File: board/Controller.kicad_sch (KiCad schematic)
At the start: 25 parts, among them U2 MP8007, U3 POE30P-50L

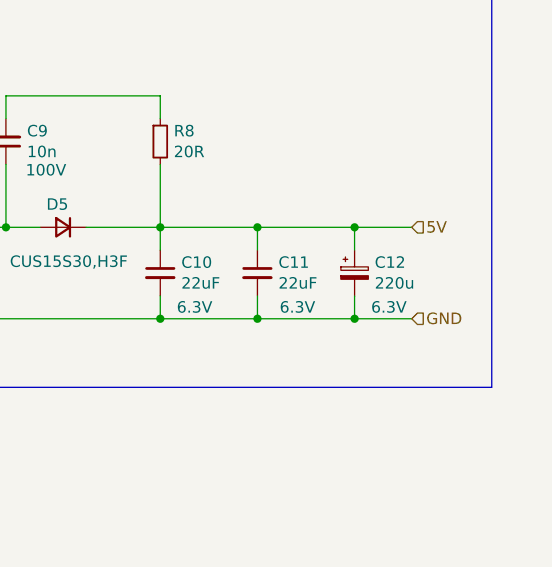
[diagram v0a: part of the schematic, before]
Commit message: added LDO
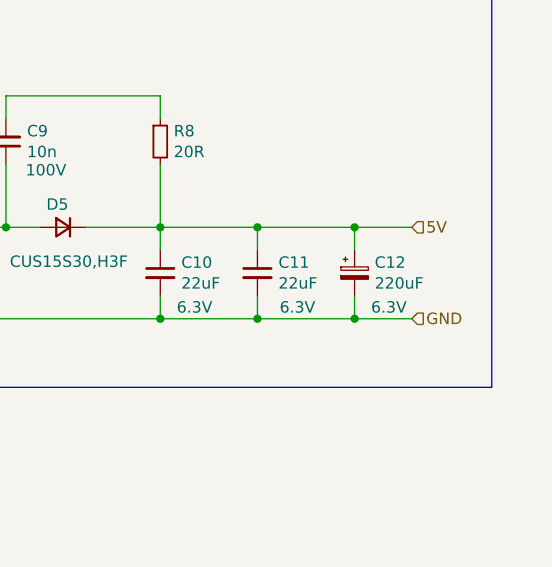
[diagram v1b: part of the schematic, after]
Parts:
- C12: value 220u -> 220uF; footprint Capacitor_Tantalum_SMD:CP_EIA-7343-31_Kemet-D -> Capacitor_SMD:CP_Elec_6.3x5.9; MPN (none) -> EEE-FK1C221XP

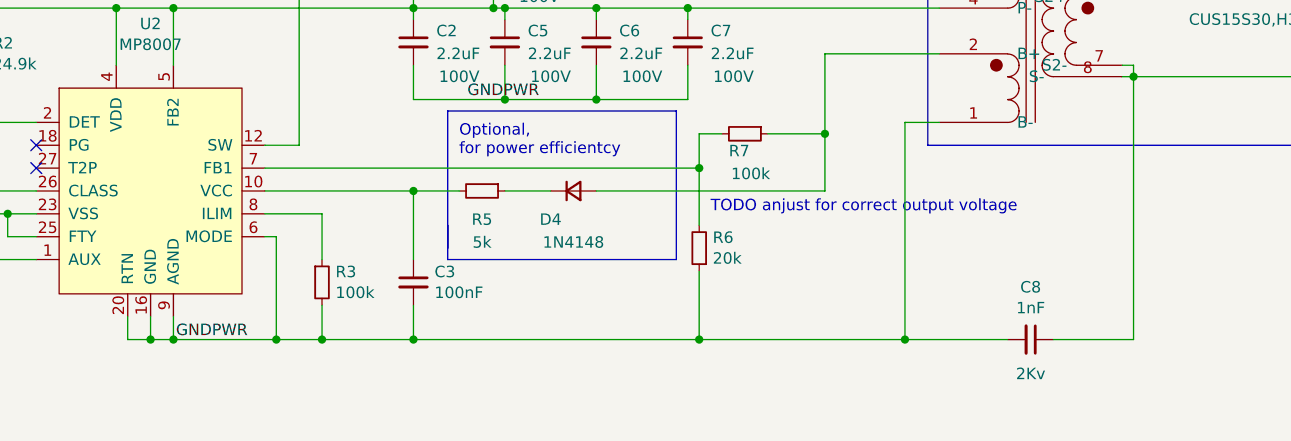
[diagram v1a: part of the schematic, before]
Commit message: tuned ILIM resistor and voltage divider of flyback
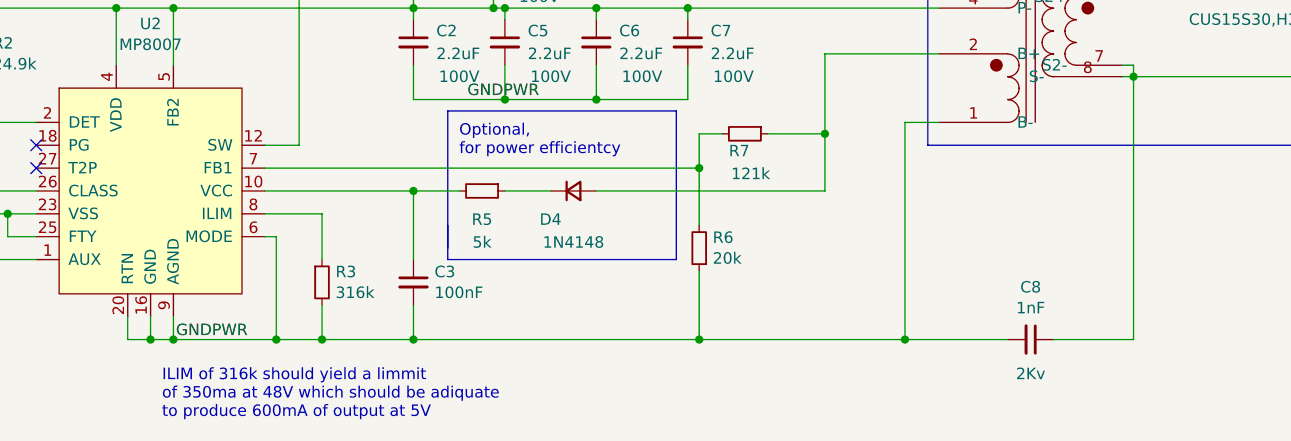
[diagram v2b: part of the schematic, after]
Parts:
- R3: value 100k -> 316k
- R7: value 100k -> 121k
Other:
- note added: "ILIM of 316k should yield a limmit of 350ma at 48V which should be adiquate to produce 600mA of output at 5V"
- note removed: "TODO anjust for correct output voltage"
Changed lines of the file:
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@@
     (effects (font (size 1.27 1.27)) (justify left bottom))
   )
-  (text "TODO anjust for correct output voltage" (at 165.1 92.71 0)
+  (text "ILIM of 316k should yield a limmit \nof 350ma at 48V which should be adiquate \nto produce 600mA of output at 5V"
+    (at 104.14 115.57 0)
     (effects (font (size 1.27 1.27)) (justify left bottom))
   )
@@
       (effects (font (size 1.27 1.27)) (justify left))
     )
-    (property "Value" "100k" (at 123.4186 101.473 0)
+    (property "Value" "316k" (at 123.4186 101.473 0)
       (effects (font (size 1.27 1.27)) (justify left))
     )
@@
       (effects (font (size 1.27 1.27)))
     )
-    (property "Value" "100k" (at 169.545 88.265 90)
-      (effects (font (size 1.27 1.27)))
-    )
+    (property "Value" "121k" (at 169.545 88.265 90)
+      (effects (font (size 1.27 1.27)))
+    )

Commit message: made bulk cap footprint larger
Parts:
- C12: footprint Capacitor_SMD:CP_Elec_6.3x5.9 -> Capacitor_SMD:CP_Elec_8x6.9
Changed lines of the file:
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@@
       (effects (font (size 1.27 1.27)) (justify left))
     )
-    (property "Footprint" "Capacitor_SMD:CP_Elec_6.3x5.9" (at 256.54 72.39 0)
+    (property "Footprint" "Capacitor_SMD:CP_Elec_8x6.9" (at 256.54 72.39 0)
       (effects (font (size 1.27 1.27)) hide)
     )

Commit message: improved docs for D4
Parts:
- D4: LCSC (none) -> C2128; MPN (none) -> 1N4148WS
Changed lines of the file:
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@@
+      (effects (font (size 1.27 1.27)) hide)
+    )
+    (property "MPN" "1N4148WS" (at 149.86 90.17 0)
+      (effects (font (size 1.27 1.27)) hide)
+    )
+    (property "LCSC" "C2128" (at 149.86 90.17 0)
       (effects (font (size 1.27 1.27)) hide)
     )

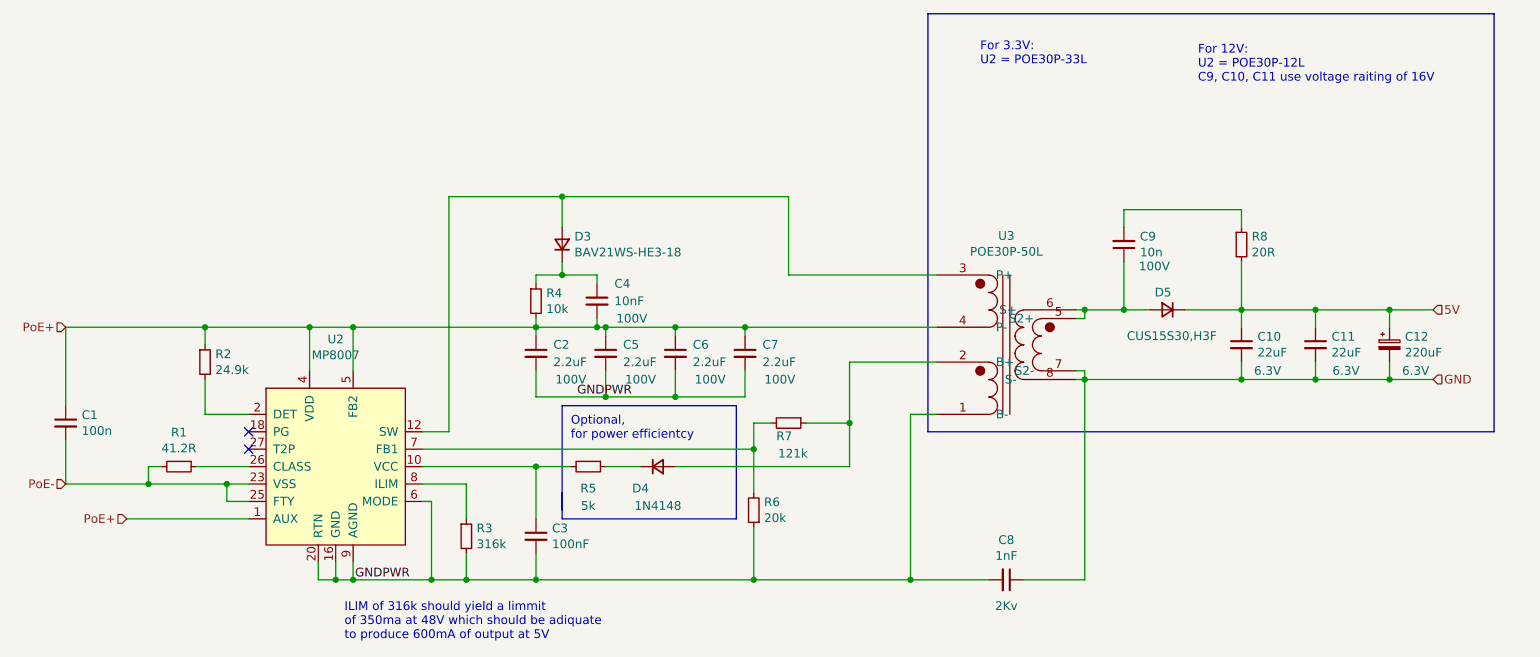
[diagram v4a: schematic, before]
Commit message: added pours for LDO and LCSC parts
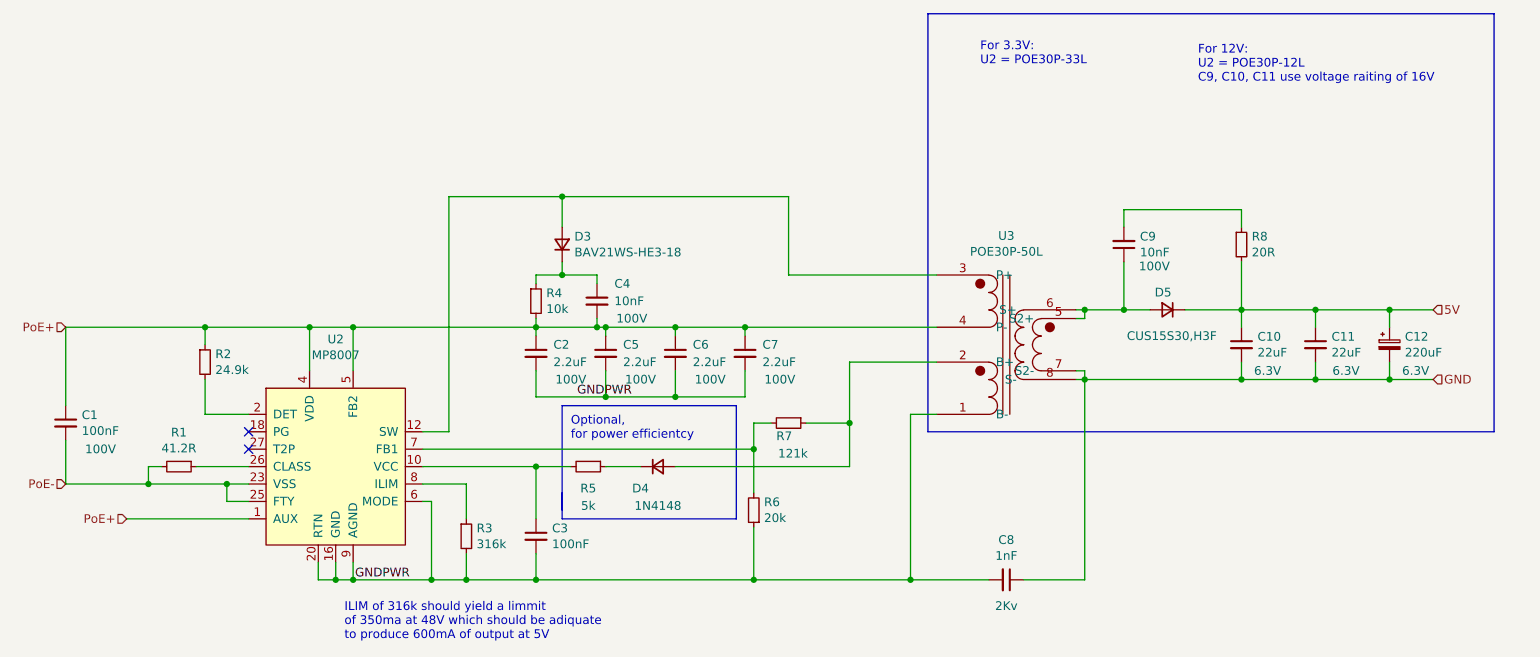
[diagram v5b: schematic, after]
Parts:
- C1: value 100n -> 100nF; Voltage (none) -> 100V
- C9: value 10n -> 10nF
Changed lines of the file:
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@@
       (effects (font (size 1.27 1.27)) hide)
     )
-    (property "Datasheet" "" (at 200.66 72.39 0)
+    (property "Datasheet" "https://www.coilcraft.com/getmedia/17806600-c691-4260-960c-34ad5e7a1dd1/poe_ep.pdf" (at 200.66 72.39 0)
       (effects (font (size 1.27 1.27)) hide)
     )
@@
       (effects (font (size 1.27 1.27)) (justify left))
     )
-    (property "Value" "100n" (at 65.8368 84.963 0)
+    (property "Value" "100nF" (at 65.8368 84.963 0)
       (effects (font (size 1.27 1.27)) (justify left))
     )
@@
       (effects (font (size 1.27 1.27)) hide)
     )
+    (property "Voltage" "100V" (at 68.58 87.63 0)
+      (effects (font (size 1.27 1.27)))
+    )
     (pin "1")
     (pin "2")
@@
       (effects (font (size 1.27 1.27)) (justify right))
     )
-    (property "Value" "10n" (at 220.1418 58.928 0)
-      (effects (font (size 1.27 1.27)) (justify right))
-    )
+    (property "Value" "10nF" (at 220.1418 58.928 0)
+      (effects (font (size 1.27 1.27)) (justify right))
+    )
